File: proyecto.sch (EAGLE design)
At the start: 35 parts, among them IC1 ADE9153AACPZ, J1 796638-3, K1 PR28-3V-360-1A-E, Q1 12.288M, U1 ESP32-PICO-MINI-02-N8R2ESP32-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

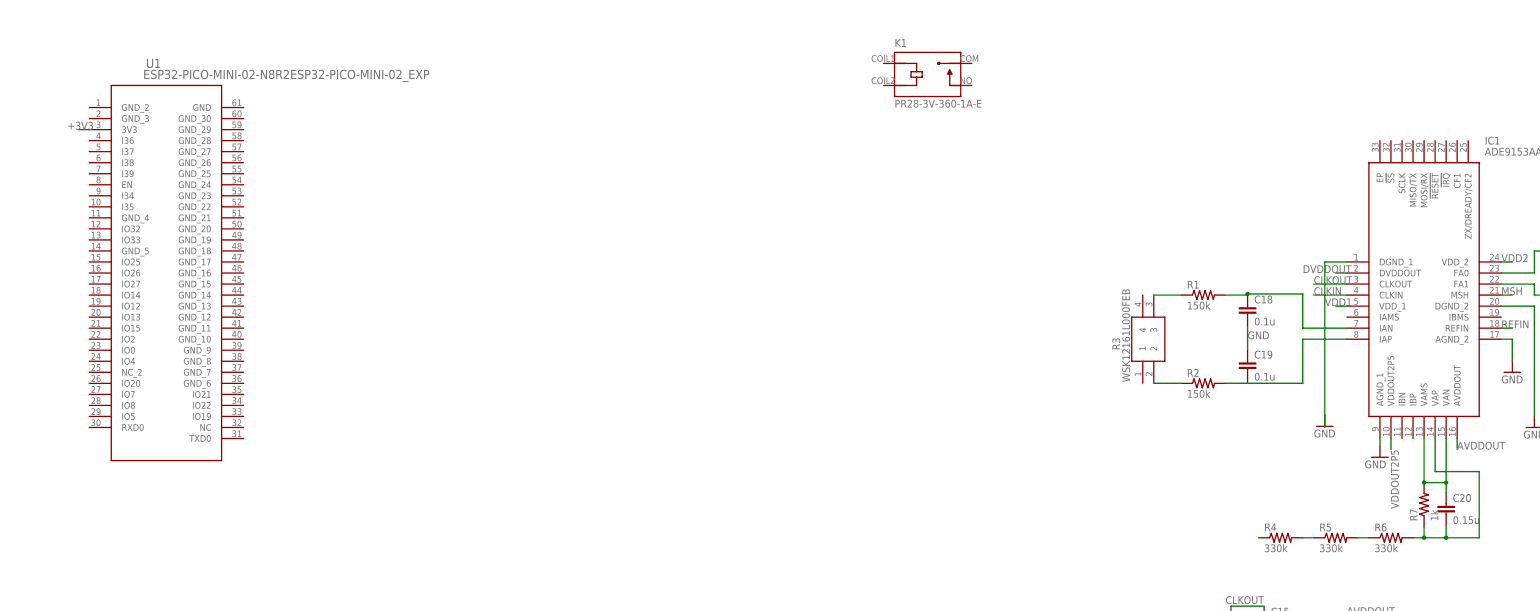
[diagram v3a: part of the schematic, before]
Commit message: Transistor de rele y headers para programar
Se añadio el transistor mosfet que va a controlar el rele, ademas del header para la programacion de microcontrolador
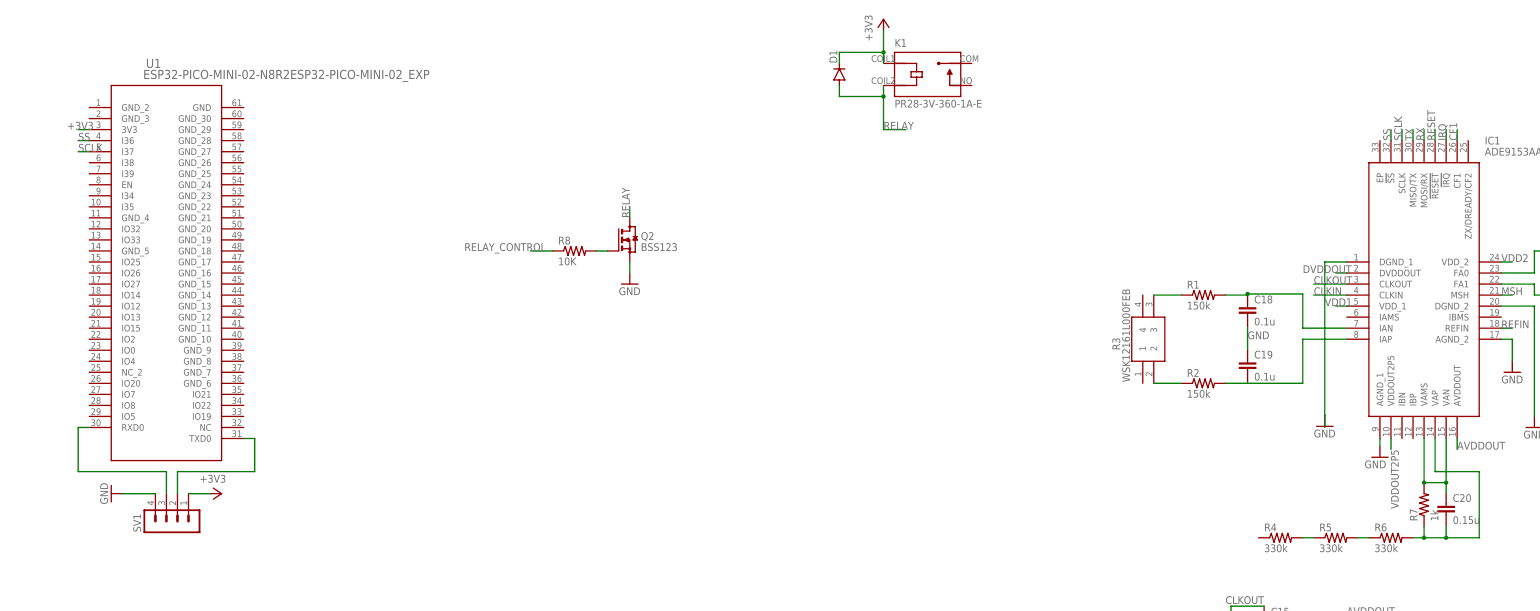
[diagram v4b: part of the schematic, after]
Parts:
- added D1: (no value), diode:DIODE-SMB
- added Q2: BSS123, transistor-small-signal:BSS123
- added R8: 10K, rcl:R-US_R0402
- added SV1: (no value), con-lstb:MA04-1
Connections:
- new net CF1: IC1.CF1
- new net IRQ: IC1.!IRQ
- new net N$11: SV1.2, U1.TXD0
- new net N$12: SV1.3, U1.RXD0
- new net N$13: Q2.G, R8.2
- new net RELAY: D1.A, K1.COIL2, Q2.D
- new net RELAY_CONTROL: R8.1
- new net RESET: IC1.!RESET
- new net RX: IC1.MOSI/RX
- new net SCLK: IC1.SCLK, U1.I37
- new net SS: IC1.!SS, U1.I36
- new net TX: IC1.MISO/TX
- net +3V3: now also D1.C, K1.COIL1, SV1.1
- net GND: now also Q2.S, SV1.4
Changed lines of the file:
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@@
 <layer number="97" name="Info" color="7" fill="1" visible="yes" active="yes"/>
 <layer number="98" name="Guide" color="6" fill="1" visible="yes" active="yes"/>
+<layer number="99" name="SpiceOrder" color="5" fill="1" visible="yes" active="yes"/>
 </layers>
 <schematic xreflabel="%F%N/%S.%C%R" xrefpart="/%S.%C%R">
@@
 <part name="GND13" library="supply1" library_urn="urn:adsk.eagle:library:371" deviceset="GND" device=""/>
 <part name="+3V2" library="supply1" library_urn="urn:adsk.eagle:library:371" deviceset="+3V3" device=""/>
+<part name="SV1" library="con-lstb" library_urn="urn:adsk.eagle:library:162" deviceset="MA04-1" device="" package3d_urn="urn:adsk.eagle:package:8337/1"/>
+<part name="+3V3" library="supply1" library_urn="urn:adsk.eagle:library:371" deviceset="+3V3" device=""/>
+<part name="GND14" library="supply1" library_urn="urn:adsk.eagle:library:371" deviceset="GND" device=""/>
+<part name="+3V4" library="supply1" library_urn="urn:adsk.eagle:library:371" deviceset="+3V3" device=""/>
+<part name="D1" library="diode" library_urn="urn:adsk.eagle:library:210" deviceset="DIODE-" device="SMB" package3d_urn="urn:adsk.eagle:package:43404/2"/>
+<part name="Q2" library="transistor-small-signal" library_urn="urn:adsk.eagle:library:401" deviceset="BSS123" device="" package3d_urn="urn:adsk.eagle:package:28738/2"/>
+<part name="GND15" library="supply1" library_urn="urn:adsk.eagle:library:371" deviceset="GND" device=""/>
+<part name="R8" library="rcl" library_urn="urn:adsk.eagle:library:334" deviceset="R-US_" device="R0402" package3d_urn="urn:adsk.eagle:package:23547/3" value="10K"/>
 </parts>
 <sheets>
@@
 <instance part="+3V2" gate="G$1" x="15.24" y="30.48" smashed="yes">
 <attribute name="VALUE" x="12.7" y="25.4" size="1.778" layer="96" rot="R90"/>
+</instance>
+<instance part="SV1" gate="1" x="129.54" y="45.72" smashed="yes" rot="R90">
+<attribute name="VALUE" x="139.7" y="44.45" size="1.778" layer="96" rot="R90"/>
+<attribute name="NAME" x="123.698" y="44.45" size="1.778" layer="95" rot="R90"/>
+</instance>
+<instance part="+3V3" gate="G$1" x="142.24" y="53.34" smashed="yes" rot="R270">
+<attribute name="VALUE" x="137.16" y="55.88" size="1.778" layer="96"/>
+</instance>
+<instance part="GND14" gate="1" x="116.84" y="53.34" smashed="yes" rot="R270">
+<attribute name="VALUE" x="114.3" y="55.88" size="1.778" layer="96" rot="R270"/>
+</instance>
+<instance part="+3V4" gate="G$1" x="294.64" y="162.56" smashed="yes">
+<attribute name="VALUE" x="292.1" y="157.48" size="1.778" layer="96" rot="R90"/>
+</instance>
+<instance part="D1" gate="G$1" x="284.48" y="149.86" smashed="yes" rot="R90">
+<attribute name="NAME" x="283.9974" y="152.4" size="1.778" layer="95" rot="R90"/>
+<attribute name="VALUE" x="286.7914" y="152.4" size="1.778" layer="96" rot="R90"/>
+</instance>
+<instance part="Q2" gate="G$1" x="236.22" y="111.76" smashed="yes">
+<attribute name="NAME" x="238.76" y="111.76" size="1.778" layer="95"/>
+<attribute name="VALUE" x="238.76" y="109.22" size="1.778" layer="96"/>
+</instance>
+<instance part="GND15" gate="1" x="236.22" y="101.6" smashed="yes">
+<attribute name="VALUE" x="233.68" y="99.06" size="1.778" layer="96"/>
+</instance>
+<instance part="R8" gate="G$1" x="223.52" y="109.22" smashed="yes">
+<attribute name="NAME" x="219.71" y="110.7186" size="1.778" layer="95"/>
+<attribute name="VALUE" x="219.71" y="105.918" size="1.778" layer="96"/>
 </instance>
 </instances>
@@
 <junction x="15.24" y="17.78"/>
 </segment>
+<segment>
+<pinref part="SV1" gate="1" pin="4"/>
+<pinref part="GND14" gate="1" pin="GND"/>
+<wire x1="127" y1="53.34" x2="119.38" y2="53.34" width="0.1524" layer="91"/>
+</segment>
+<segment>
+<pinref part="GND15" gate="1" pin="GND"/>
+<pinref part="Q2" gate="G$1" pin="S"/>
+<wire x1="236.22" y1="104.14" x2="236.22" y2="106.68" width="0.1524" layer="91"/>
+</segment>
 </net>
 <net name="VDD1" class="0">
@@
 <wire x1="111.76" y1="137.16" x2="109.22" y2="137.16" width="0.1524" layer="91"/>
 <label x="106.68" y="137.16" size="1.778" layer="95"/>
+</segment>
+<segment>
+<pinref part="SV1" gate="1" pin="1"/>
+<pinref part="+3V3" gate="G$1" pin="+3V3"/>
+<wire x1="134.62" y1="53.34" x2="139.7" y2="53.34" width="0.1524" layer="91"/>
+</segment>
+<segment>
+<pinref part="K1" gate="G$1" pin="COIL1"/>
+<pinref part="+3V4" gate="G$1" pin="+3V3"/>
+<wire x1="294.64" y1="152.4" x2="294.64" y2="154.94" width="0.1524" layer="91"/>
+<pinref part="D1" gate="G$1" pin="C"/>
+<wire x1="294.64" y1="154.94" x2="294.64" y2="160.02" width="0.1524" layer="91"/>
+<wire x1="284.48" y1="152.4" x2="284.48" y2="154.94" width="0.1524" layer="91"/>
+<wire x1="284.48" y1="154.94" x2="294.64" y2="154.94" width="0.1524" layer="91"/>
+<junction x="294.64" y="154.94"/>
 </segment>
 </net>
@@
 </segment>
 </net>
+<net name="N$11" class="0">
+<segment>
+<pinref part="SV1" gate="1" pin="2"/>
+<wire x1="132.08" y1="53.34" x2="132.08" y2="58.42" width="0.1524" layer="91"/>
+<wire x1="132.08" y1="58.42" x2="149.86" y2="58.42" width="0.1524" layer="91"/>
+<wire x1="149.86" y1="58.42" x2="149.86" y2="66.04" width="0.1524" layer="91"/>
+<pinref part="U1" gate="A" pin="TXD0"/>
+<wire x1="149.86" y1="66.04" x2="147.32" y2="66.04" width="0.1524" layer="91"/>
+</segment>
+</net>
+<net name="N$12" class="0">
+<segment>
+<pinref part="SV1" gate="1" pin="3"/>
+<wire x1="129.54" y1="53.34" x2="129.54" y2="58.42" width="0.1524" layer="91"/>
+<wire x1="129.54" y1="58.42" x2="109.22" y2="58.42" width="0.1524" layer="91"/>
+<wire x1="109.22" y1="58.42" x2="109.22" y2="68.58" width="0.1524" layer="91"/>
+<pinref part="U1" gate="A" pin="RXD0"/>
+<wire x1="109.22" y1="68.58" x2="111.76" y2="68.58" width="0.1524" layer="91"/>
+</segment>
+</net>
+<net name="SS" class="0">
+<segment>
+<pinref part="IC1" gate="G$1" pin="!SS"/>
+<wire x1="411.48" y1="134.62" x2="411.48" y2="137.16" width="0.1524" layer="91"/>
+<label x="411.48" y="134.62" size="1.778" layer="95" rot="R90"/>
+</segment>
+<segment>
+<pinref part="U1" gate="A" pin="I36"/>
+<wire x1="111.76" y1="134.62" x2="109.22" y2="134.62" width="0.1524" layer="91"/>
+<label x="109.22" y="134.62" size="1.778" layer="95"/>
+</segment>
+</net>
+<net name="SCLK" class="0">
+<segment>
+<pinref part="IC1" gate="G$1" pin="SCLK"/>
+<wire x1="414.02" y1="134.62" x2="414.02" y2="137.16" width="0.1524" layer="91"/>
+<label x="414.02" y="134.62" size="1.778" layer="95" rot="R90"/>
+</segment>
+<segment>
+<pinref part="U1" gate="A" pin="I37"/>
+<wire x1="111.76" y1="132.08" x2="109.22" y2="132.08" width="0.1524" layer="91"/>
+<label x="109.22" y="132.08" size="1.778" layer="95"/>
+</segment>
+</net>
+<net name="TX" class="0">
+<segment>
+<pinref part="IC1" gate="G$1" pin="MISO/TX"/>
+<wire x1="416.56" y1="134.62" x2="416.56" y2="137.16" width="0.1524" layer="91"/>
+<label x="416.56" y="134.62" size="1.778" layer="95" rot="R90"/>
+</segment>
+</net>
+<net name="RX" class="0">
+<segment>
+<pinref part="IC1" gate="G$1" pin="MOSI/RX"/>
+<wire x1="419.1" y1="134.62" x2="419.1" y2="137.16" width="0.1524" layer="91"/>
+<label x="419.1" y="134.62" size="1.778" layer="95" rot="R90"/>
+</segment>
+</net>
+<net name="RESET" class="0">
+<segment>
+<pinref part="IC1" gate="G$1" pin="!RESET"/>
+<wire x1="421.64" y1="134.62" x2="421.64" y2="137.16" width="0.1524" layer="91"/>
+<label x="421.64" y="134.62" size="1.778" layer="95" rot="R90"/>
+</segment>
+</net>
+<net name="IRQ" class="0">
+<segment>
+<pinref part="IC1" gate="G$1" pin="!IRQ"/>
+<wire x1="424.18" y1="134.62" x2="424.18" y2="137.16" width="0.1524" layer="91"/>
+<label x="424.18" y="134.62" size="1.778" layer="95" rot="R90"/>
+</segment>
+</net>
+<net name="CF1" class="0">
+<segment>
+<pinref part="IC1" gate="G$1" pin="CF1"/>
+<wire x1="426.72" y1="134.62" x2="426.72" y2="137.16" width="0.1524" layer="91"/>
+<label x="426.72" y="134.62" size="1.778" layer="95" rot="R90"/>
+</segment>
+</net>
+<net name="RELAY" class="0">
+<segment>
+<pinref part="K1" gate="G$1" pin="COIL2"/>
+<wire x1="294.64" y1="147.32" x2="294.64" y2="144.78" width="0.1524" layer="91"/>
+<wire x1="294.64" y1="144.78" x2="294.64" y2="137.16" width="0.1524" layer="91"/>
+<wire x1="294.64" y1="137.16" x2="299.72" y2="137.16" width="0.1524" layer="91"/>
+<label x="294.64" y="137.16" size="1.778" layer="95"/>
+<pinref part="D1" gate="G$1" pin="A"/>
+<wire x1="284.48" y1="147.32" x2="284.48" y2="144.78" width="0.1524" layer="91"/>
+<wire x1="284.48" y1="144.78" x2="294.64" y2="144.78" width="0.1524" layer="91"/>
+<junction x="294.64" y="144.78"/>
+</segment>
+<segment>
+<pinref part="Q2" gate="G$1" pin="D"/>
+<wire x1="236.22" y1="116.84" x2="236.22" y2="119.38" width="0.1524" layer="91"/>
+<label x="236.22" y="116.84" size="1.778" layer="95" rot="R90"/>
+</segment>
+</net>
+<net name="N$13" class="0">
+<segment>
+<pinref part="R8" gate="G$1" pin="2"/>
+<pinref part="Q2" gate="G$1" pin="G"/>
+<wire x1="228.6" y1="109.22" x2="231.14" y2="109.22" width="0.1524" layer="91"/>
+</segment>
+</net>
+<net name="RELAY_CONTROL" class="0">
+<segment>
+<pinref part="R8" gate="G$1" pin="1"/>
+<wire x1="218.44" y1="109.22" x2="213.36" y2="109.22" width="0.1524" layer="91"/>
+<label x="198.12" y="109.22" size="1.778" layer="95"/>
+</segment>
+</net>

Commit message: Creacion de pistas y nuevos componentes
Se hicieron las lineas criticas del circuito como lo son la fuente de alimentacion, linea, neutro, linea de medicion de corriente de la carga. Ademas se hicieron poligonos con el fin de conectar una capa con la otra.

Ademas se añadio el circuito del Enable del microcontrolador
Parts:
- added C23: 0.1u, rcl:C-EUC0201
- added R9: 10K, rcl:R-US_R1206
- added S1: (no value), switch-omron:10-XX
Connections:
- new net CARGA: J1.1
- new net CARGA_M: K1.NO, R3.1
- new net EN: R9.1, U1.EN
- new net LINEA: K1.COM, PS1.VAC_IN_(L)
- new net N$14: C23.1, R9.2, S1.S
- new net NEUTRO: J1.3, PS1.VAC_IN_(N)
- new net TIERRA: J1.2
- net GND: now also C23.2, S1.P
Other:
- moved on the sheet: J1, PS1
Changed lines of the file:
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@@
 <part name="GND15" library="supply1" library_urn="urn:adsk.eagle:library:371" deviceset="GND" device=""/>
 <part name="R8" library="rcl" library_urn="urn:adsk.eagle:library:334" deviceset="R-US_" device="R0402" package3d_urn="urn:adsk.eagle:package:23547/3" value="10K"/>
+<part name="S1" library="switch-omron" library_urn="urn:adsk.eagle:library:377" deviceset="10-XX" device="" package3d_urn="urn:adsk.eagle:package:27496/1"/>
+<part name="C23" library="rcl" library_urn="urn:adsk.eagle:library:334" deviceset="C-EU" device="C0201" package3d_urn="urn:adsk.eagle:package:23690/2" value="0.1u"/>
+<part name="R9" library="rcl" library_urn="urn:adsk.eagle:library:334" deviceset="R-US_" device="R1206" package3d_urn="urn:adsk.eagle:package:23540/2" value="10K"/>
+<part name="GND16" library="supply1" library_urn="urn:adsk.eagle:library:371" deviceset="GND" device=""/>
 </parts>
 <sheets>
@@
 <attribute name="SHEET" x="230.505" y="5.08" size="2.54" layer="94"/>
 </instance>
-<instance part="J1" gate="G$1" x="33.02" y="149.86" smashed="yes">
-<attribute name="NAME" x="49.53" y="157.48" size="1.778" layer="95" align="center-left"/>
-<attribute name="VALUE" x="49.53" y="154.94" size="1.778" layer="96" align="center-left"/>
-</instance>
-<instance part="PS1" gate="G$1" x="12.7" y="111.76" smashed="yes">
-<attribute name="NAME" x="46.99" y="119.38" size="1.778" layer="95" align="center-left"/>
-<attribute name="VALUE" x="46.99" y="116.84" size="1.778" layer="96" align="center-left"/>
+<instance part="J1" gate="G$1" x="497.84" y="147.32" smashed="yes">
+<attribute name="NAME" x="514.35" y="154.94" size="1.778" layer="95" align="center-left"/>
+<attribute name="VALUE" x="514.35" y="152.4" size="1.778" layer="96" align="center-left"/>
+</instance>
+<instance part="PS1" gate="G$1" x="17.78" y="111.76" smashed="yes">
+<attribute name="NAME" x="52.07" y="119.38" size="1.778" layer="95" align="center-left"/>
+<attribute name="VALUE" x="52.07" y="116.84" size="1.778" layer="96" align="center-left"/>
 </instance>
 <instance part="K1" gate="G$1" x="304.8" y="149.86" smashed="yes">
@@
 <attribute name="VALUE" x="384.81" y="4.572" size="1.778" layer="96"/>
 </instance>
-<instance part="+3V1" gate="G$1" x="53.34" y="127" smashed="yes">
-<attribute name="VALUE" x="50.8" y="121.92" size="1.778" layer="96" rot="R90"/>
-</instance>
-<instance part="GND12" gate="1" x="53.34" y="104.14" smashed="yes">
-<attribute name="VALUE" x="50.8" y="101.6" size="1.778" layer="96"/>
+<instance part="+3V1" gate="G$1" x="58.42" y="127" smashed="yes">
+<attribute name="VALUE" x="55.88" y="121.92" size="1.778" layer="96" rot="R90"/>
+</instance>
+<instance part="GND12" gate="1" x="58.42" y="104.14" smashed="yes">
+<attribute name="VALUE" x="55.88" y="101.6" size="1.778" layer="96"/>
 </instance>
 <instance part="C17" gate="G$1" x="452.12" y="104.14" smashed="yes">
@@
 <attribute name="NAME" x="219.71" y="110.7186" size="1.778" layer="95"/>
 <attribute name="VALUE" x="219.71" y="105.918" size="1.778" layer="96"/>
+</instance>
+<instance part="S1" gate="1" x="48.26" y="25.4" smashed="yes" rot="R270">
+<attribute name="NAME" x="45.72" y="31.75" size="1.778" layer="95"/>
+<attribute name="VALUE" x="51.435" y="29.21" size="1.778" layer="96"/>
+</instance>
+<instance part="C23" gate="G$1" x="49.784" y="17.78" smashed="yes" rot="R270">
+<attribute name="NAME" x="50.165" y="16.256" size="1.778" layer="95" rot="R270"/>
+<attribute name="VALUE" x="45.085" y="16.256" size="1.778" layer="96" rot="R270"/>
+</instance>
+<instance part="R9" gate="G$1" x="60.96" y="25.4" smashed="yes" rot="MR0">
+<attribute name="NAME" x="64.77" y="26.8986" size="1.778" layer="95" rot="MR0"/>
+<attribute name="VALUE" x="64.77" y="22.098" size="1.778" layer="96" rot="MR0"/>
+</instance>
+<instance part="GND16" gate="1" x="38.1" y="10.16" smashed="yes">
+<attribute name="VALUE" x="35.56" y="7.62" size="1.778" layer="96"/>
 </instance>
 </instances>
@@
 <segment>
 <pinref part="PS1" gate="G$1" pin="-VOUT"/>
-<wire x1="50.8" y1="109.22" x2="53.34" y2="109.22" width="0.1524" layer="91"/>
+<wire x1="55.88" y1="109.22" x2="58.42" y2="109.22" width="0.1524" layer="91"/>
 <pinref part="GND12" gate="1" pin="GND"/>
-<wire x1="53.34" y1="109.22" x2="53.34" y2="106.68" width="0.1524" layer="91"/>
+<wire x1="58.42" y1="109.22" x2="58.42" y2="106.68" width="0.1524" layer="91"/>
 </segment>
 <segment>
@@
 <wire x1="236.22" y1="104.14" x2="236.22" y2="106.68" width="0.1524" layer="91"/>
 </segment>
+<segment>
+<pinref part="S1" gate="1" pin="P"/>
+<pinref part="GND16" gate="1" pin="GND"/>
+<wire x1="43.18" y1="25.4" x2="38.1" y2="25.4" width="0.1524" layer="91"/>
+<wire x1="38.1" y1="25.4" x2="38.1" y2="17.78" width="0.1524" layer="91"/>
+<pinref part="C23" gate="G$1" pin="2"/>
+<wire x1="38.1" y1="17.78" x2="38.1" y2="12.7" width="0.1524" layer="91"/>
+<wire x1="44.704" y1="17.78" x2="38.1" y2="17.78" width="0.1524" layer="91"/>
+<junction x="38.1" y="17.78"/>
+</segment>
 </net>
 <net name="VDD1" class="0">
@@
 <segment>
 <pinref part="PS1" gate="G$1" pin="+VOUT"/>
-<wire x1="50.8" y1="111.76" x2="53.34" y2="111.76" width="0.1524" layer="91"/>
+<wire x1="55.88" y1="111.76" x2="58.42" y2="111.76" width="0.1524" layer="91"/>
 <pinref part="+3V1" gate="G$1" pin="+3V3"/>
-<wire x1="53.34" y1="111.76" x2="53.34" y2="124.46" width="0.1524" layer="91"/>
+<wire x1="58.42" y1="111.76" x2="58.42" y2="124.46" width="0.1524" layer="91"/>
 </segment>
 <segment>
@@
 </segment>
 </net>
+<net name="N$14" class="0">
+<segment>
+<pinref part="C23" gate="G$1" pin="1"/>
+<wire x1="52.324" y1="17.78" x2="55.88" y2="17.78" width="0.1524" layer="91"/>
+<pinref part="R9" gate="G$1" pin="2"/>
+<wire x1="55.88" y1="17.78" x2="55.88" y2="25.4" width="0.1524" layer="91"/>
+<pinref part="S1" gate="1" pin="S"/>
+<wire x1="55.88" y1="25.4" x2="53.34" y2="25.4" width="0.1524" layer="91"/>
+<junction x="55.88" y="25.4"/>
+</segment>
+</net>
+<net name="EN" class="0">
+<segment>
+<pinref part="U1" gate="A" pin="EN"/>
+<wire x1="111.76" y1="124.46" x2="109.22" y2="124.46" width="0.1524" layer="91"/>
+<label x="109.22" y="124.46" size="1.778" layer="95"/>
+</segment>
+<segment>
+<pinref part="R9" gate="G$1" pin="1"/>
+<wire x1="66.04" y1="25.4" x2="68.58" y2="25.4" width="0.1524" layer="91"/>
+<label x="66.04" y="25.4" size="1.778" layer="95"/>
+</segment>
+</net>
+<net name="LINEA" class="0">
+<segment>
+<pinref part="PS1" gate="G$1" pin="VAC_IN_(L)"/>
+<wire x1="17.78" y1="109.22" x2="15.24" y2="109.22" width="0.1524" layer="91"/>
+<label x="10.16" y="109.22" size="1.778" layer="95"/>
+</segment>
+<segment>
+<pinref part="K1" gate="G$1" pin="COM"/>
+<wire x1="314.96" y1="152.4" x2="317.5" y2="152.4" width="0.1524" layer="91"/>
+<label x="317.5" y="152.4" size="1.778" layer="95"/>
+</segment>
+</net>
+<net name="TIERRA" class="0">
+<segment>
+<pinref part="J1" gate="G$1" pin="2"/>
+<wire x1="497.84" y1="144.78" x2="495.3" y2="144.78" width="0.1524" layer="91"/>
+<label x="490.22" y="144.78" size="1.778" layer="95"/>
+</segment>
+</net>
+<net name="CARGA" class="0">
+<segment>
+<pinref part="J1" gate="G$1" pin="1"/>
+<wire x1="497.84" y1="147.32" x2="495.3" y2="147.32" width="0.1524" layer="91"/>
+<label x="490.22" y="147.32" size="1.778" layer="95"/>
+</segment>
+</net>
+<net name="NEUTRO" class="0">
+<segment>
+<pinref part="J1" gate="G$1" pin="3"/>
+<wire x1="497.84" y1="142.24" x2="495.3" y2="142.24" width="0.1524" layer="91"/>
+<label x="487.68" y="142.24" size="1.778" layer="95"/>
+</segment>
+<segment>
+<pinref part="PS1" gate="G$1" pin="VAC_IN_(N)"/>
+<wire x1="17.78" y1="111.76" x2="15.24" y2="111.76" width="0.1524" layer="91"/>
+<label x="7.62" y="111.76" size="1.778" layer="95"/>
+</segment>
+</net>
+<net name="CARGA_M" class="0">
+<segment>
+<pinref part="K1" gate="G$1" pin="NO"/>
+<wire x1="314.96" y1="147.32" x2="317.5" y2="147.32" width="0.1524" layer="91"/>
+<label x="317.5" y="147.32" size="1.778" layer="95"/>
+</segment>
+<segment>
+<pinref part="R3" gate="G$1" pin="1"/>
+<wire x1="354.33" y1="78.74" x2="354.33" y2="76.708" width="0.1524" layer="91"/>
+<label x="353.06" y="66.04" size="1.778" layer="95" rot="R90"/>
+</segment>
+</net>
